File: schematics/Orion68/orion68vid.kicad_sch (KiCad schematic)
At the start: 0 parts

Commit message: Schematics update
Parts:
- added C4: 10pF, Capacitor_THT:C_Disc_D4.3mm_W1.9mm_P5.00mm, symbol Device:C
- added J9: Euro96pin, ConnPdSilva:conn_euro96, symbol ConnPdSilva:ConnEuro96
- added Q5: 2N3904, Package_TO_SOT_THT:TO-92_Inline, symbol Transistor_BJT:2N3904
- added R34, R35, R36, R37, R38, R39, R40, R41, R42, R43, R44, R45, R46, R47, R48, R49: 1k, symbol Device:R
- added R50: 470R, Resistor_THT:R_Axial_DIN0204_L3.6mm_D1.6mm_P5.08mm_Horizontal, symbol Device:R
- added R53: 1k, Resistor_THT:R_Axial_DIN0204_L3.6mm_D1.6mm_P5.08mm_Horizontal, symbol Device:R
- added U18, U19: 74HC245, symbol 74xx:74HC245
- added U20: 24LC256, symbol Memory_EEPROM:24LC256
- added U21: ~, symbol pdSilva:Raspi pi pico
- added U24: GAL16V8, symbol Logic_Programmable:GAL16V8
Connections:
- new net: R42.2, U19.18 (B0)
- new net: C4.1, Q5.2 (B), R53.1
- new net: C4.2, R53.2, U24.19 (IO1)
- new net: R39.2, U18.13 (B5)
- new net: R50.1, U18.20 (VCC), U19.20 (VCC), U20.8 (VCC), U21.36 (3V3(OUT))
- new net: R45.2, U19.15 (B3)
- new net: R44.2, U19.16 (B2)
- new net: R47.1, U21.26 (GP20)
- new net: R34.2, U18.18 (B0)
- new net: R43.2, U19.17 (B1)
- new net: R46.2, U19.14 (B4)
- new net: R36.2, U18.16 (B2)
- new net: U18.1 (A->B), U18.10 (GND), U18.19 (CE), U19.1 (A->B), U19.10 (GND), U19.11 (B7), U19.12 (B6), U19.13 (B5), U19.19 (CE), U19.7 (A5), U19.8 (A6), U19.9 (A7), U20.1 (A0), U20.2 (A1), U20.3 (A2), U20.4 (GND), U20.7 (WP), U21.13 (GND), U21.18 (GND), U21.23 (GND), U21.28 (GND), U21.3 (GND), U21.33 (GND), U21.38 (GND), U21.8 (GND)
- new net: U19.2 (A0), U21.11 (GP8)
- new net: U19.3 (A1), U21.12 (GP9)
- new net: U19.4 (A2), U21.14 (GP10)
- new net: U19.5 (A3), U21.15 (GP11)
- new net: U19.6 (A4), U21.16 (GP12)
- new net: R49.1, U21.24 (GP18)
- new net: R48.1, U21.25 (GP19)
- new net: R41.2, U18.11 (B7)
- new net: R37.2, U18.15 (B3)
- new net: R38.2, U18.14 (B4)
- new net: U18.2 (A0), U21.1 (GP0)
- new net: U18.9 (A7), U21.10 (GP7)
- new net: U18.3 (A1), U21.2 (GP1)
- new net: U18.4 (A2), U21.4 (GP2)
- new net: U18.5 (A3), U21.5 (GP3)
- new net: U18.6 (A4), U21.6 (GP4)
- new net: U18.7 (A5), U21.7 (GP5)
- new net: U18.8 (A6), U21.9 (GP6)
- new net: R40.2, U18.12 (B6)
- new net: R35.2, U18.17 (B1)
- new net +12V: J9.92
- new net +5V: J9.1, J9.33, J9.65, U21.39 (VSYS), U24.20 (VCC)
- new net -5V: J9.94
- new net ALE: J9.73
- new net BA0: J9.18
- new net BA1: J9.19, R42.1
- new net BA10: J9.28
- new net BA11: J9.29
- new net BA12: J9.30
- new net BA13: J9.31
- new net BA14: J9.63
- new net BA15: J9.62, U24.1 (I1/CLK)
- new net BA16: J9.61, U24.2 (I2)
- new net BA17: J9.60, U24.3 (I3)
- new net BA18: J9.59, U24.4 (I4)
- new net BA19: J9.58, U24.5 (I5)
- new net BA2: J9.20, R43.1
- new net BA20: J9.57
- new net BA21: J9.56
- new net BA22: J9.55
- new net BA23: J9.54
- new net BA3: J9.21, R44.1
- new net BA4: J9.22, R45.1
- new net BA5: J9.23, R46.1
- new net BA6: J9.24
- new net BA7: J9.25
- new net BA8: J9.26
- new net BA9: J9.27
- new net BD0: J9.2, R34.1
- new net BD1: J9.3, R35.1
- new net BD10: J9.12
- new net BD11: J9.13
- new net BD12: J9.14
- new net BD13: J9.15
- new net BD14: J9.16
- new net BD15: J9.17
- new net BD2: J9.4, R36.1
- new net BD3: J9.5, R37.1
- new net BD4: J9.6, R38.1
- new net BD5: J9.7, R39.1
- new net BD6: J9.8, R40.1
- new net BD7: J9.9, R41.1
- new net BD8: J9.10
- new net BD9: J9.11
- new net BLUE: R49.2
- new net BOOTIN: J9.87
- new net B/AS: U24.8 (I8)
- new net B/LDS: U24.6 (I6)
- new net B/cpurd: J9.45
- new net B/cpurw: J9.46
- new net B/cpuwr: U24.7 (I7)
- new net CPU_CLK: J9.81
- new net CRUCLK: J9.35
- new net CRUIN: J9.36
- new net CRUOUT: J9.37
- new net DBIN: J9.38
- new net DT/R: J9.75
- new net E: J9.34
- new net GND: J9.32, J9.64, J9.93, J9.95, J9.96, Q5.1 (E), U24.10 (GND)
- new net GREEN: R48.2
- new net HLDA: J9.52
- new net HSYNC: U21.21 (GP16)
- new net IAQ: J9.39
- new net IC3: J9.47
- new net IRQ2: J9.48
- new net IRQ3: J9.49
- new net IRQ4: J9.50
- new net IRQ5: J9.89
- new net IRQ6: J9.90
- new net IRQ7: J9.91
- new net M/IO: J9.76
- new net NMI: J9.41
- new net PWR_GOOD: J9.88
- new net RDY: J9.44
- new net RESET: J9.67
- new net Red: R47.2
- new net Res9: J9.69
- new net SCL: U20.6 (SCL), U21.20 (GP15)
- new net SDA: U20.5 (SDA), U21.19 (GP14)
- new net TICK_IN: J9.86
- new net VSYNC: U21.22 (GP17)
- new net /AS: J9.43
- new net /BERR: J9.68
- new net /CS: Q5.3 (C), R50.2, U21.17 (GP13)
- new net /DEN: J9.74
- new net /HALT: J9.53
- new net /HOLD: J9.42
- new net /INTA: J9.72
- new net /INTR: J9.40
- new net /IO_CS: J9.85, U24.9 (I9)
- new net /LDS: J9.70
- new net /M1: J9.79
- new net /RESET: J9.66
- new net /RFSH: J9.80
- new net /RST: J9.51
- new net /SSO: J9.77
- new net /UDS: J9.71
- new net /WAIT: J9.78
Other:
- note added: "19 18 17 16 | 15 1 0 0 0 | 0 = F80000 1 0 0 0 | 1 = F88000 1 0 0 1 | 0 = F90000 1 0 0 1 | 1 = F98000 1 0 1 0 | 0 = FA0000 1 0 1 0 | 1 = FA8000 1 0 1 1 | 0 = FB0000 1 0 1 1 | 1 = FB8000 pino 1 (A0) = A15 do 68000 pino 2 (A1) = A16 do 68000 pino 3 (A2) = A17 do 68000 pino 4 (/E0) = A18 do 68000 pino 5 (/E1) = /LDS R/W /AS do 68000 pino 6 (E2) = A19 do 68000 com isso a saida pino 7 /Y7 só deve ser a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"

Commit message: Schematics update
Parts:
- U18, U19, U24: footprint (none) -> Package_DIP:DIP-20_W7.62mm
- U20: footprint (none) -> Package_DIP:DIP-8_W7.62mm
- U21: footprint (none) -> Package_DIP:DIP-40_W15.24mm
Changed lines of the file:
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@@
 			)
 		)
-		(property "Footprint" ""
+		(property "Footprint" "Package_DIP:DIP-20_W7.62mm"
 			(at 201.93 93.98 0)
 			(effects
@@
 			)
 		)
-		(property "Footprint" ""
+		(property "Footprint" "Package_DIP:DIP-20_W7.62mm"
 			(at 59.69 137.16 0)
 			(effects
@@
 			)
 		)
-		(property "Footprint" ""
+		(property "Footprint" "Package_DIP:DIP-40_W15.24mm"
 			(at 104.14 69.85 0)
 			(effects
@@
 			)
 		)
-		(property "Footprint" ""
+		(property "Footprint" "Package_DIP:DIP-20_W7.62mm"
 			(at 59.69 86.36 0)
 			(effects
@@
 			)
 		)
-		(property "Footprint" ""
+		(property "Footprint" "Package_DIP:DIP-8_W7.62mm"
 			(at 85.09 173.99 0)
 			(effects

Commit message: Schematic update
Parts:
- removed J9: Euro96pin, ConnPdSilva:conn_euro96, symbol ConnPdSilva:ConnEuro96
- added J5: Euro96pin, ConnPdSilva:conn_euro96, symbol ConnPdSilva:ConnEuro96
- R47, R48, R49: value 1k -> 330R
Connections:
- net +12V: now also J5.92
- net +5V: now also J5.1, J5.33, J5.65
- net -5V: now also J5.94
- net ALE: now also J5.73
- net BA0: now also J5.18
- net BA1: now also J5.19
- net BA10: now also J5.28
- net BA11: now also J5.29
- net BA12: now also J5.30
- net BA13: now also J5.31
- net BA14: now also J5.63
- net BA15: now also J5.62
- net BA16: now also J5.61
- net BA17: now also J5.60
- net BA18: now also J5.59
- net BA19: now also J5.58
- net BA2: now also J5.20
- net BA20: now also J5.57
- net BA21: now also J5.56
- net BA22: now also J5.55
- net BA23: now also J5.54
- net BA3: now also J5.21
- net BA4: now also J5.22
- net BA5: now also J5.23
- net BA6: now also J5.24
- net BA7: now also J5.25
- net BA8: now also J5.26
- net BA9: now also J5.27
- net BD0: now also J5.2
- net BD1: now also J5.3
- net BD10: now also J5.12
- net BD11: now also J5.13
- net BD12: now also J5.14
- net BD13: now also J5.15
- net BD14: now also J5.16
- net BD15: now also J5.17
- net BD2: now also J5.4
- net BD3: now also J5.5
- net BD4: now also J5.6
- net BD5: now also J5.7
- net BD6: now also J5.8
- net BD7: now also J5.9
- net BD8: now also J5.10
- net BD9: now also J5.11
- net BOOTIN: now also J5.87
- net B/AS: now also J5.43
- net B/LDS: now also J5.70
- net B/cpurd: now also J5.45
- net B/cpuwr: now also J5.46
- net CPU_CLK: now also J5.81
- net CRUCLK: now also J5.35
- net CRUIN: now also J5.36
- net CRUOUT: now also J5.37
- net DBIN: now also J5.38
- net DT/R: now also J5.75
- net E: now also J5.34
- net GND: now also J5.32, J5.64, J5.93, J5.95, J5.96
- net HLDA: now also J5.52
- net IAQ: now also J5.39
- net IC3: now also J5.47
- net IRQ2: now also J5.48
- net IRQ3: now also J5.49
- net IRQ4: now also J5.50
- net IRQ5: now also J5.89
- net IRQ6: now also J5.90
- net IRQ7: now also J5.91
- net M/IO: now also J5.76
- net NMI: now also J5.41
- net PWR_GOOD: now also J5.88
- net RDY: now also J5.44
- net RESET: now also J5.67
- net Res9: now also J5.69
- net TICK_IN: now also J5.86
- net /BERR: now also J5.68
- net /DEN: now also J5.74
- net /HALT: now also J5.53
- net /HOLD: now also J5.42
- net /INTA: now also J5.72
- net /INTR: now also J5.40
- net /IO_CS: now also J5.85
- net /M1: now also J5.79
- net /RESET: now also J5.66
- net /RFSH: now also J5.80
- net /RST: now also J5.51
- net /SSO: now also J5.77
- net /WAIT: now also J5.78
- new net B/UDS: J5.71

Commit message: Updating
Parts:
- R300: renamed from R34; footprint (none) -> Resistor_THT:R_Axial_DIN0204_L3.6mm_D1.6mm_P5.08mm_Horizontal
- R301: renamed from R35; footprint (none) -> Resistor_THT:R_Axial_DIN0204_L3.6mm_D1.6mm_P5.08mm_Horizontal
- R302: renamed from R36; footprint (none) -> Resistor_THT:R_Axial_DIN0204_L3.6mm_D1.6mm_P5.08mm_Horizontal
- R303: renamed from R37; footprint (none) -> Resistor_THT:R_Axial_DIN0204_L3.6mm_D1.6mm_P5.08mm_Horizontal
- R304: renamed from R38; footprint (none) -> Resistor_THT:R_Axial_DIN0204_L3.6mm_D1.6mm_P5.08mm_Horizontal
- R305: renamed from R39; footprint (none) -> Resistor_THT:R_Axial_DIN0204_L3.6mm_D1.6mm_P5.08mm_Horizontal
- R306: renamed from R40; footprint (none) -> Resistor_THT:R_Axial_DIN0204_L3.6mm_D1.6mm_P5.08mm_Horizontal
- R307: renamed from R41; footprint (none) -> Resistor_THT:R_Axial_DIN0204_L3.6mm_D1.6mm_P5.08mm_Horizontal
- R308: renamed from R42; footprint (none) -> Resistor_THT:R_Axial_DIN0204_L3.6mm_D1.6mm_P5.08mm_Horizontal
- R309: renamed from R43; footprint (none) -> Resistor_THT:R_Axial_DIN0204_L3.6mm_D1.6mm_P5.08mm_Horizontal
- R310: renamed from R44; footprint (none) -> Resistor_THT:R_Axial_DIN0204_L3.6mm_D1.6mm_P5.08mm_Horizontal
- R311: renamed from R45; footprint (none) -> Resistor_THT:R_Axial_DIN0204_L3.6mm_D1.6mm_P5.08mm_Horizontal
- R312: renamed from R46; footprint (none) -> Resistor_THT:R_Axial_DIN0204_L3.6mm_D1.6mm_P5.08mm_Horizontal
- R313: renamed from R47; footprint (none) -> Resistor_THT:R_Axial_DIN0204_L3.6mm_D1.6mm_P5.08mm_Horizontal
- R314: renamed from R48; footprint (none) -> Resistor_THT:R_Axial_DIN0204_L3.6mm_D1.6mm_P5.08mm_Horizontal
- R315: renamed from R49; footprint (none) -> Resistor_THT:R_Axial_DIN0204_L3.6mm_D1.6mm_P5.08mm_Horizontal
- renumbered C4 to C300, J5 to J300, Q5 to Q300, R50 to R316, R53 to R317, U21 to U300, U18 to U301, U19 to U302, U20 to U303, U24 to U304
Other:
- note added: "Video card board - 300"
- note removed: "Video card board"

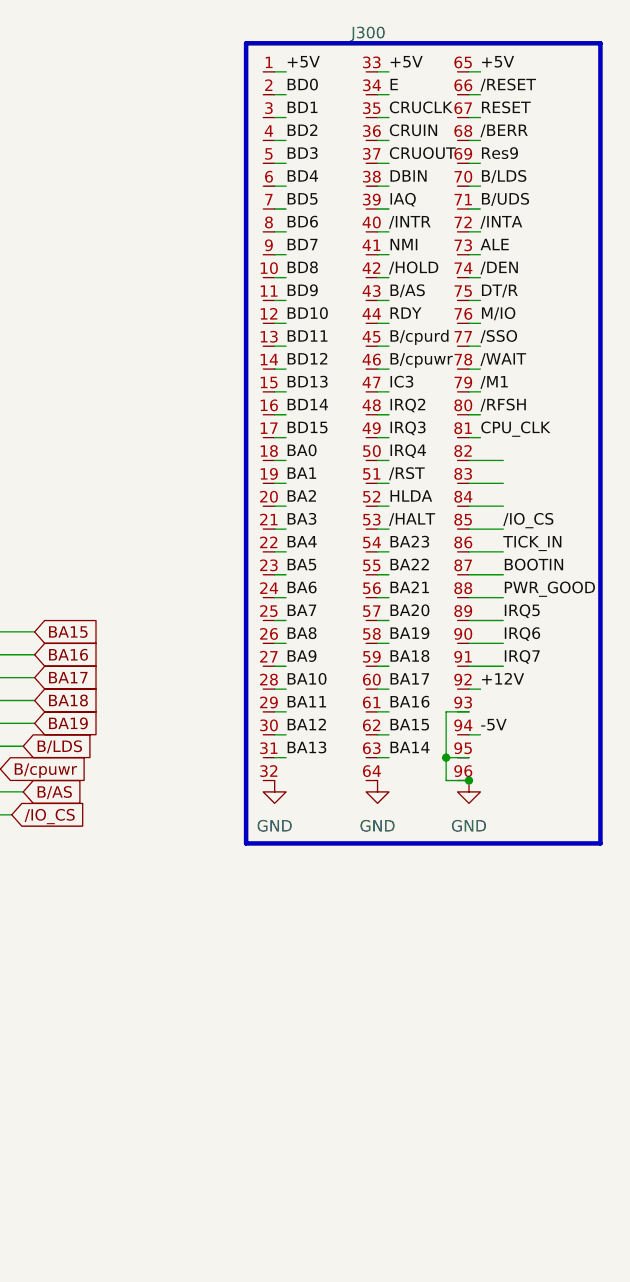
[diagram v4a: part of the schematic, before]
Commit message: Schematic verified to board
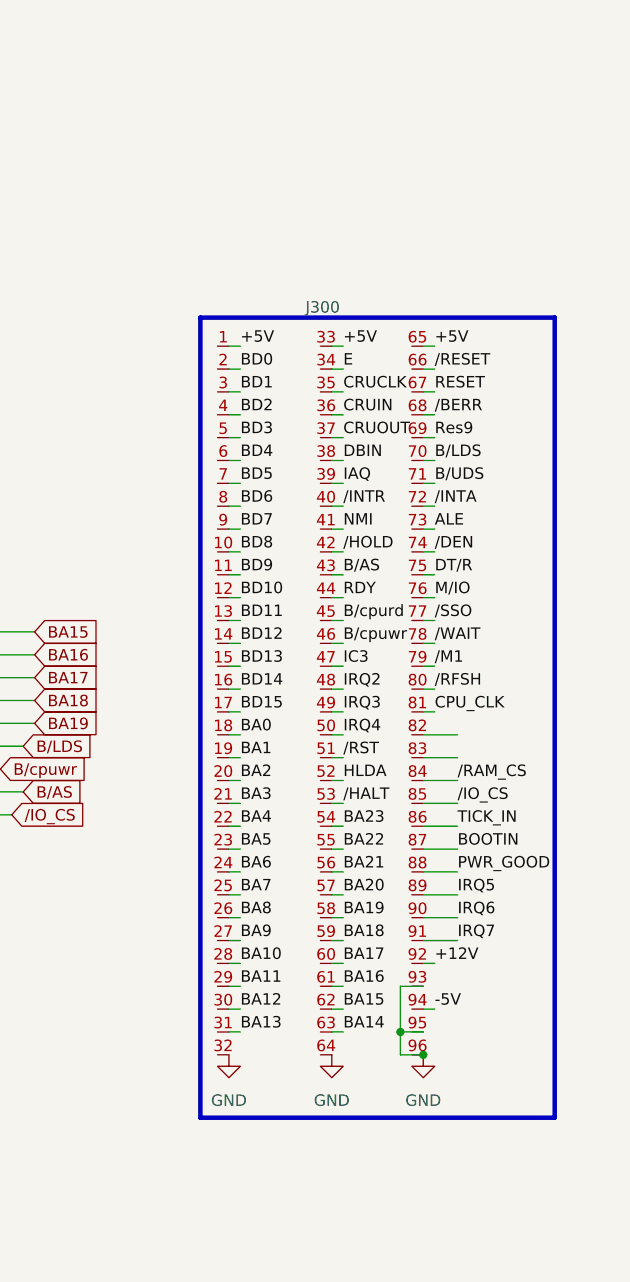
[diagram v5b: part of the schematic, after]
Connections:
- net /RAM_CS: now reaches J300.84

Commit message: Cpu board fixed and running
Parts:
- removed C300: 10pF, Capacitor_THT:C_Disc_D4.3mm_W1.9mm_P5.00mm, symbol Device:C
- removed Q300: 2N3904, Package_TO_SOT_THT:TO-92_Inline, symbol Transistor_BJT:2N3904
- added Q4: 2N7000, Package_TO_SOT_THT:TO-92_Inline, symbol Transistor_FET:2N7000
- R316: value 470R -> 10K
- R317: value 1k -> 10k
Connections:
- net +5V: now also R317.2
- net /CS: now also Q4.1 (S)
- net /IO_CS: no longer J300.85
- net at R317.1: now also U304.19 (IO1), Q4.3 (D)
- net +3,3V: now reaches R316.1, U300.36 (3V3(OUT)), U301.20 (VCC), U302.20 (VCC), U303.8 (VCC)
- net +3,3V: now also Q4.2 (G)
- net /RAM_CS: no longer names the net of J300.84
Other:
- moved on the sheet: R316, R317

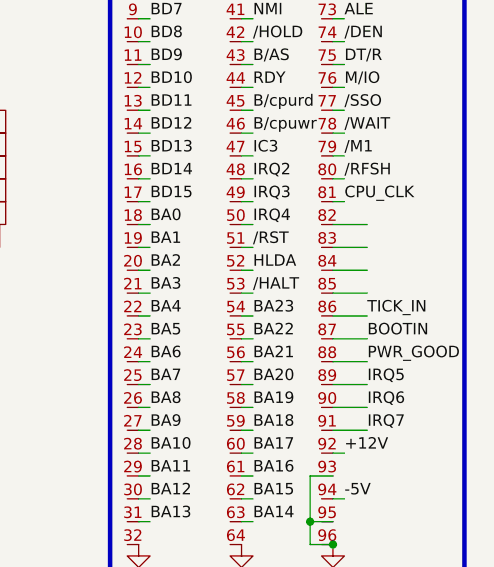
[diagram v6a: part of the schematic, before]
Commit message: A20 bug fixed, missing serial CSA, running ok
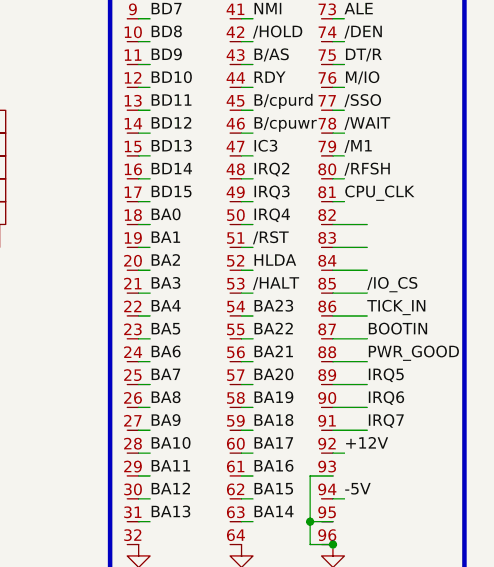
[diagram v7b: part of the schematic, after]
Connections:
- net /IO_CS: now also J300.85
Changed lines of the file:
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@@
+		)
+	)
+	(label "{slash}IO_CS"
+		(at 266.7 100.33 0)
+		(effects
+			(font
+				(size 1.27 1.27)
+			)
+			(justify left bottom)
 		)
 	)

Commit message: updating
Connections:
- net B/LDS: no longer U304.6 (I6)
- net GND: now also U304.11 (I10/~{OE})
- net /IO_CS: no longer U304.9 (I9)
- net A20: now reaches U304.12 (IO8)
- net A21: now reaches U304.13 (IO7)
- net A22: now reaches U304.14 (IO6)
- new net A23: U304.9 (I9)
- new net /LDS: U304.6 (I6)
